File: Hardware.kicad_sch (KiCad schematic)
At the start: 29 parts, among them J1 Conn_01x06_Socket, J5 Conn_01x05_Socket, Q1 BC849, Q2 BC849, SW1 Push_Button, SW2 Push_Button, U1 ESP32-WROOM-32, U9 AMS1117-3.3

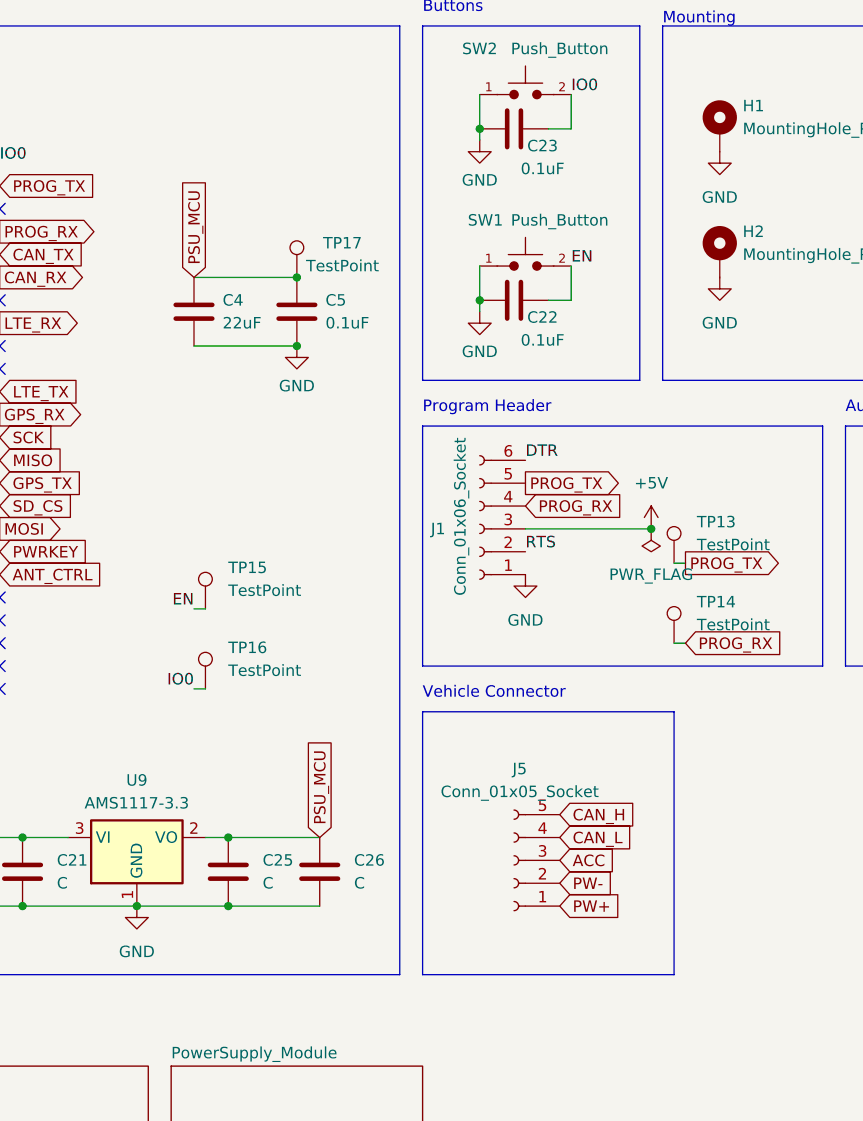
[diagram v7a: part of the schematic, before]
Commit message: added footprint for a7670e
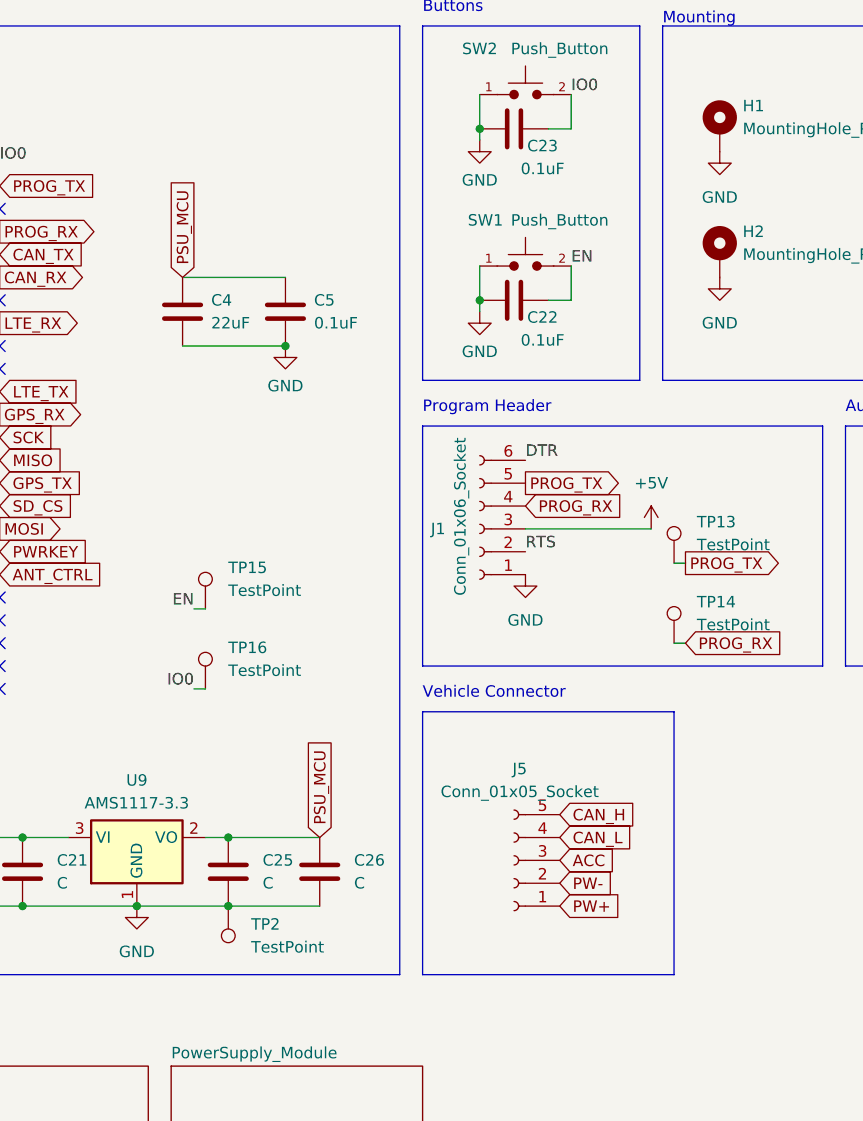
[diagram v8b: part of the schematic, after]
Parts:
- removed TP17: TestPoint, symbol Connector:TestPoint
- added TP2: TestPoint, symbol Connector:TestPoint
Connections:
- net GND: now also TP2.1
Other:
- moved on the sheet: C4, C5
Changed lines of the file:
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@@
 	)
 	(junction
-		(at 132.08 73.66)
-		(diameter 0)
-		(color 0 0 0 0)
-	)
-	(junction
-		(at 92.71 45.72)
-		(diameter 0)
-		(color 0 0 0 0)
-	)
-	(junction
 		(at 162.56 82.55)
 		(diameter 0)
@@
 	)
 	(junction
-		(at 92.71 53.34)
+		(at 91.44 53.34)
 		(diameter 0)
 		(color 0 0 0 0)
@@
 	(wire
 		(pts
-			(xy 81.28 53.34) (xy 92.71 53.34)
+			(xy 80.01 53.34) (xy 91.44 53.34)
 		)
 		(stroke
@@
 	(wire
 		(pts
-			(xy 81.28 45.72) (xy 92.71 45.72)
+			(xy 80.01 45.72) (xy 91.44 45.72)
 		)
 		(stroke
@@
 	(global_label "PSU_MCU"
 		(shape input)
-		(at 81.28 45.72 90)
+		(at 80.01 45.72 90)
 		(fields_autoplaced yes)
 		(effects
@@
 		)
 		(property "Intersheetrefs" "${INTERSHEET_REFS}"
-			(at 81.28 33.9053 90)
+			(at 80.01 33.9053 90)
 			(effects
 				(font
@@
 	(symbol
 		(lib_id "power:GND")
-		(at 92.71 53.34 0)
+		(at 91.44 53.34 0)
 		(unit 1)
 		(exclude_from_sim no)
@@
 		(fields_autoplaced yes)
 		(property "Reference" "#PWR08"
-			(at 92.71 59.69 0)
+			(at 91.44 59.69 0)
 			(effects
 				(font
@@
 		)
 		(property "Value" "GND"
-			(at 92.71 57.785 0)
+			(at 91.44 57.785 0)
 			(effects
 				(font
@@
 		)
 		(property "Footprint" ""
-			(at 92.71 53.34 0)
+			(at 91.44 53.34 0)
 			(effects
 				(font
@@
 		)
 		(property "Datasheet" ""
-			(at 92.71 53.34 0)
+			(at 91.44 53.34 0)
 			(effects
 				(font
@@
 		)
 		(property "Description" ""
-			(at 92.71 53.34 0)
+			(at 91.44 53.34 0)
 			(effects
 				(font
@@
 	)
 	(symbol
-		(lib_id "Connector:TestPoint")
-		(at 92.71 45.72 0)
+		(lib_id "Device:C")
+		(at 95.25 111.76 0)
 		(unit 1)
 		(exclude_from_sim no)
@@
 		(on_board yes)
 		(dnp no)
-		(property "Reference" "TP17"
-			(at 97.79 41.91 0)
+		(fields_autoplaced yes)
+		(property "Reference" "C26"
+			(at 99.06 110.4899 0)
 			(effects
 				(font
 					(size 1.27 1.27)
 				)
+				(justify left)
 			)
 		)
-		(property "Value" "TestPoint"
-			(at 97.79 44.45 0)
+		(property "Value" "C"
+			(at 99.06 113.0299 0)
 			(effects
 				(font
 					(size 1.27 1.27)
 				)
+				(justify left)
 			)
 		)
 		(property "Footprint" ""
-			(at 97.79 45.72 0)
+			(at 96.2152 115.57 0)
 			(effects
 				(font
@@
 		)
 		(property "Datasheet" "~"
-			(at 97.79 45.72 0)
+			(at 95.25 111.76 0)
 			(effects
 				(font
@@
 			)
 		)
-		(property "Description" "test point"
-			(at 92.71 45.72 0)
+		(property "Description" "Unpolarized capacitor"
+			(at 95.25 111.76 0)
 			(effects
 				(font
@@
 			)
 		)
+		(pin "2"
+		)
 		(pin "1"
 		)
@@
 			(project "Hardware"
 				(path "/f04ee758-a926-48b7-b458-286a696c3ef4"
-					(reference "TP17")
+					(reference "C26")
 					(unit 1)
 				)
@@
 	)
 	(symbol
-		(lib_id "Device:C")
-		(at 95.25 111.76 0)
+		(lib_id "Connector:TestPoint")
+		(at 85.09 115.57 180)
 		(unit 1)
 		(exclude_from_sim no)
@@
 		(dnp no)
 		(fields_autoplaced yes)
-		(property "Reference" "C26"
-			(at 99.06 110.4899 0)
+		(property "Reference" "TP2"
+			(at 87.63 117.6019 0)
 			(effects
 				(font
 					(size 1.27 1.27)
 				)
-				(justify left)
+				(justify right)
 			)
 		)
-		(property "Value" "C"
-			(at 99.06 113.0299 0)
+		(property "Value" "TestPoint"
+			(at 87.63 120.1419 0)
 			(effects
 				(font
 					(size 1.27 1.27)
 				)
-				(justify left)
+				(justify right)
 			)
 		)
 		(property "Footprint" ""
-			(at 96.2152 115.57 0)
+			(at 80.01 115.57 0)
 			(effects
 				(font
@@
 		)
 		(property "Datasheet" "~"
-			(at 95.25 111.76 0)
+			(at 80.01 115.57 0)
 			(effects
 				(font
@@
 			)
 		)
-		(property "Description" "Unpolarized capacitor"
-			(at 95.25 111.76 0)
+		(property "Description" "test point"
+			(at 85.09 115.57 0)
 			(effects
 				(font
@@
 			)
 		)
-		(pin "2"
-		)
 		(pin "1"
 		)
@@
 			(project "Hardware"
 				(path "/f04ee758-a926-48b7-b458-286a696c3ef4"
-					(reference "C26")
+					(reference "TP2")
 					(unit 1)
 				)
@@
 	)
 	(symbol
-		(lib_id "power:PWR_FLAG")
-		(at 132.08 73.66 180)
-		(unit 1)
-		(exclude_from_sim no)
-		(in_bom yes)
-		(on_board yes)
-		(dnp no)
-		(fields_autoplaced yes)
-		(property "Reference" "#FLG01"
-			(at 132.08 75.565 0)
-			(effects
-				(font
-					(size 1.27 1.27)
-				)
-				(hide yes)
-			)
-		)
-		(property "Value" "PWR_FLAG"
-			(at 132.08 78.74 0)
-			(effects
-				(font
-					(size 1.27 1.27)
-				)
-			)
-		)
-		(property "Footprint" ""
-			(at 132.08 73.66 0)
-			(effects
-				(font
-					(size 1.27 1.27)
-				)
-				(hide yes)
-			)
-		)
-		(property "Datasheet" "~"
-			(at 132.08 73.66 0)
-			(effects
-				(font
-					(size 1.27 1.27)
-				)
-				(hide yes)
-			)
-		)
-		(property "Description" "Special symbol for telling ERC where power comes from"
-			(at 132.08 73.66 0)
-			(effects
-				(font
-					(size 1.27 1.27)
-				)
-				(hide yes)
-			)
-		)
-		(pin "1"
-		)
-		(instances
-			(project "Hardware"
-				(path "/f04ee758-a926-48b7-b458-286a696c3ef4"
-					(reference "#FLG01")
-					(unit 1)
-				)
-			)
-		)
-	)
-	(symbol
 		(lib_id "Device:C")
 		(at 116.84 48.26 90)
@@
 	(symbol
 		(lib_id "Device:C")
-		(at 92.71 49.53 0)
+		(at 91.44 49.53 0)
 		(unit 1)
 		(exclude_from_sim no)
@@
 		(fields_autoplaced yes)
 		(property "Reference" "C5"
-			(at 95.885 48.26 0)
+			(at 94.615 48.26 0)
 			(effects
 				(font
@@
 		)
 		(property "Value" "0.1uF"
-			(at 95.885 50.8 0)
+			(at 94.615 50.8 0)
 			(effects
 				(font
@@
 		)
 		(property "Footprint" "Capacitor_SMD:C_0805_2012Metric_Pad1.18x1.45mm_HandSolder"
-			(at 93.6752 53.34 0)
+			(at 92.4052 53.34 0)
 			(effects
 				(font
@@
 		)
 		(property "Datasheet" "~"
-			(at 92.71 49.53 0)
+			(at 91.44 49.53 0)
 			(effects
 				(font
@@
 		)
 		(property "Description" ""
-			(at 92.71 49.53 0)
+			(at 91.44 49.53 0)
 			(effects
 				(font
@@
 	(symbol
 		(lib_id "Device:C")
-		(at 81.28 49.53 0)
+		(at 80.01 49.53 0)
 		(unit 1)
 		(exclude_from_sim no)
@@
 		(fields_autoplaced yes)
 		(property "Reference" "C4"
-			(at 84.455 48.26 0)
+			(at 83.185 48.26 0)
 			(effects
 				(font
@@
 		)
 		(property "Value" "22uF"
-			(at 84.455 50.8 0)
+			(at 83.185 50.8 0)
 			(effects
 				(font
@@
 		)
 		(property "Footprint" "Capacitor_SMD:C_1206_3216Metric_Pad1.33x1.80mm_HandSolder"
-			(at 82.2452 53.34 0)
+			(at 80.9752 53.34 0)
 			(effects
 				(font
@@
 		)
 		(property "Datasheet" "~"
-			(at 81.28 49.53 0)
+			(at 80.01 49.53 0)
 			(effects
 				(font
@@
 		)
 		(property "Description" ""
-			(at 81.28 49.53 0)
+			(at 80.01 49.53 0)
 			(effects
 				(font
